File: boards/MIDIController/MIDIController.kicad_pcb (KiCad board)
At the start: 2 copper layers, 29 parts, among them J4 KeyboardCtrl, J5 TechnicsCtrl, J6 StopLeftCtrl, J7 StopRightCtrl, J9 PanelCtrl

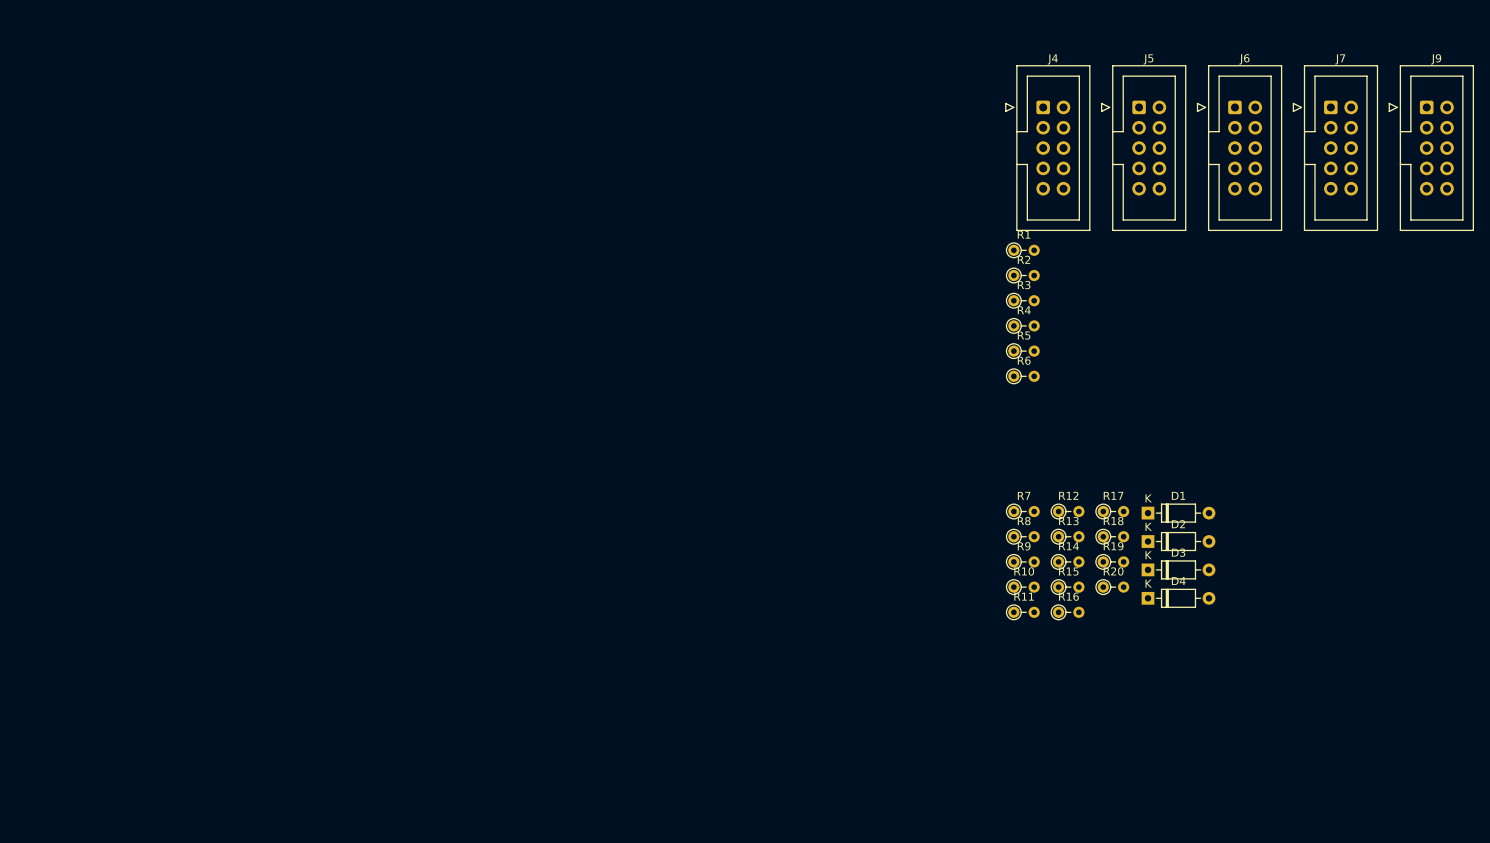
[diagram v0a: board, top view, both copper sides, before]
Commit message: Added Optocoupler and RS232 converter to UART board lines.
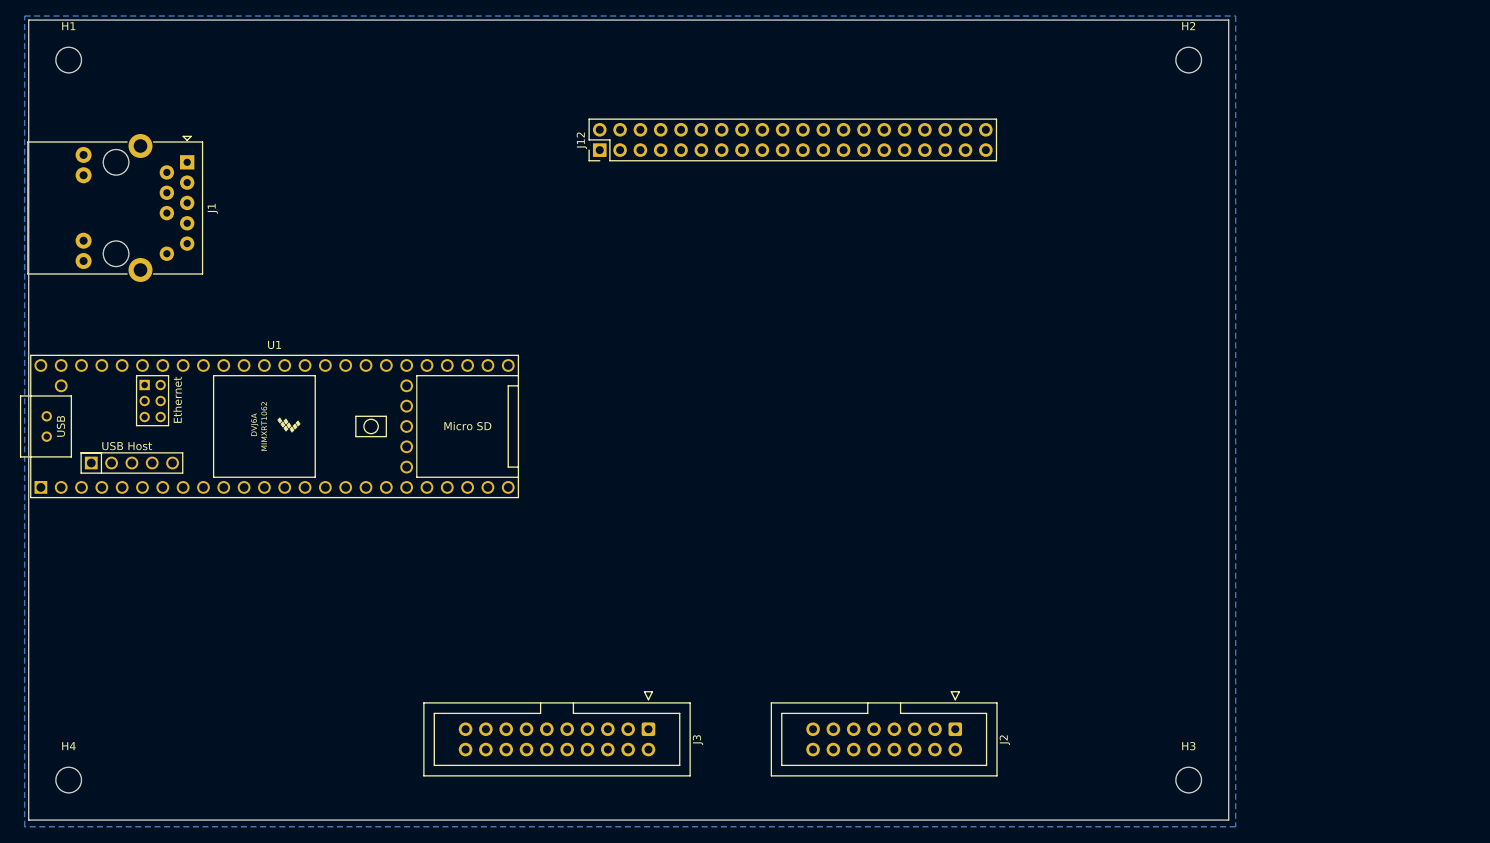
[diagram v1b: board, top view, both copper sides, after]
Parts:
- removed D1, D2, D3, D4: 1N4148, Diode_THT:D_DO-35_SOD27_P7.62mm_Horizontal
- removed J4: KeyboardCtrl, Connector_IDC:IDC-Header_2x05_P2.54mm_Vertical
- removed J5: TechnicsCtrl, Connector_IDC:IDC-Header_2x05_P2.54mm_Vertical
- removed J6: StopLeftCtrl, Connector_IDC:IDC-Header_2x05_P2.54mm_Vertical
- removed J7: StopRightCtrl, Connector_IDC:IDC-Header_2x05_P2.54mm_Vertical
- removed J9: PanelCtrl, Connector_IDC:IDC-Header_2x05_P2.54mm_Vertical
- removed R1, R11, R12, R13, R14, R15, R16, R17, R18, R19, R2, R20, R3, R4, R5, R6: 220, Resistor_THT:R_Axial_DIN0204_L3.6mm_D1.6mm_P2.54mm_Vertical
- removed R10, R7, R8, R9: 10k, Resistor_THT:R_Axial_DIN0204_L3.6mm_D1.6mm_P2.54mm_Vertical
- added H1: MountingHole, MountingHole:MountingHole_3.2mm_M3, F.Cu at (71.5, 50.2)
- added H2: MountingHole, MountingHole:MountingHole_3.2mm_M3, F.Cu at (211.5, 50.2)
- added H3: MountingHole, MountingHole:MountingHole_3.2mm_M3, F.Cu at (211.5, 140.2)
- added H4: MountingHole, MountingHole:MountingHole_3.2mm_M3, F.Cu at (71.5, 140.2)
- added J1: RJ45_Abracon_ARJP11A-MASA-B-A-EMU2, Connector_RJ:RJ45_Abracon_ARJP11A-MA_Horizontal, F.Cu at (86.4, 63.0)
- added J12: Raspberry_Pi_2_3, Connector_PinHeader_2.54mm:PinHeader_2x20_P2.54mm_Vertical, F.Cu at (137.9, 61.5)
- added J2: MIDICon, Connector_IDC:IDC-Header_2x08_P2.54mm_Vertical, F.Cu at (182.4, 133.9)
- added J3: IO_Boards, Connector_IDC:IDC-Header_2x10_P2.54mm_Vertical, F.Cu at (144.0, 133.9)
- added U1: Teensy4.1, Teensy:Teensy41, F.Cu at (97.3, 96.0)
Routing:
- added copper zone on B.Cu, net GND
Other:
- board outline added: 150 x 100 mm

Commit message: Updated MidiController PCB footprints
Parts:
- removed J12: Raspberry_Pi_2_3, Connector_PinHeader_2.54mm:PinHeader_2x20_P2.54mm_Vertical
- added C1: 100nF, Capacitor_THT:C_Disc_D4.3mm_W1.9mm_P5.00mm, F.Cu at (177.1, 92.5)
- added C2: 10uF, Capacitor_THT:CP_Radial_D7.5mm_P2.50mm, F.Cu at (179.0, 86.2)
- added C3: 100nF, Capacitor_THT:C_Disc_D4.3mm_W1.9mm_P5.00mm, F.Cu at (167.0, 93.1)
- added J4: USB_A, Connector_USB:USB_A_Molex_67643_Horizontal, F.Cu at (79.5, 119.4)
- added J5: I2S_Data, Connector_PinHeader_2.54mm:PinHeader_1x08_P2.54mm_Vertical, F.Cu at (163.1, 84.0)
- added J6: I2C_Pwr, Connector_PinHeader_2.54mm:PinHeader_1x08_P2.54mm_Vertical, F.Cu at (153.9, 84.3)
- added J7: Raspberry_Pi_2_3, Connector_PinHeader_2.54mm:PinHeader_2x20_P2.54mm_Vertical, F.Cu at (137.4, 61.5)
- added J8: RJ45_Amphenol_RJMG1BD3B8K1ANR, Connector_RJ:RJ45_Amphenol_RJMG1BD3B8K1ANR, F.Cu at (84.1, 64.8)
- added RN1: 1k, Resistor_THT:R_Array_SIP9, F.Cu at (151.7, 126.0)
- J1: value RJ45_Abracon_ARJP11A-MASA-B-A-EMU2 -> Ctrl; footprint Connector_RJ:RJ45_Abracon_ARJP11A-MA_Horizontal -> Connector_PinHeader_2.54mm:PinHeader_1x03_P2.54mm_Vertical
- moved J1 84.0 mm to (167.7, 84.0), turned to 0 degrees
- moved U1 1.80 mm to (97.0, 94.2)
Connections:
- J1 pad 1: unconnected-(J1-TD+-Pad1) -> Net-(J1-Pin_1)
- J1 pad 2: unconnected-(J1-TD--Pad2) -> Net-(J1-Pin_2)
- J1 pad 3: unconnected-(J1-RD+-Pad3) -> Net-(J1-Pin_3)
- J3 pad 1: /INT1 -> /Int_Panel
- J3 pad 10: /SDA -> +12V
- J3 pad 11: /INT5 -> /Int_Kbd
- J3 pad 12: /SCL -> GND
- J3 pad 14: +3.3V -> GND
- J3 pad 17: /RXD3 -> /RXD4
- J3 pad 18: GND -> +5V
- J3 pad 19: /RXD4 -> /RXD3
- J3 pad 2: +12V -> +3.3V
- J3 pad 20: GND -> +5V
- J3 pad 3: /INT2 -> /Int_StopLeft
- J3 pad 4: +12V -> /SDA
- J3 pad 5: /INT4 -> /Int_StopRight
- J3 pad 6: +5V -> /SCL
- J3 pad 7: /INT3 -> /Int_ToeStud
- J3 pad 8: +5V -> +12V
- J3 pad 9: /INT6 -> /Int_Technics
- U1 pad 12: unconnected-(U1-10_CS_MQSR-Pad12) -> /RPI_CS
- U1 pad 13: unconnected-(U1-11_MOSI_CTX1-Pad13) -> /RPI_MOSI
- U1 pad 14: unconnected-(U1-12_MISO_MQSL-Pad14) -> /RPI_MISO
- U1 pad 25: unconnected-(U1-33_MCLK2-Pad25) -> /I2S_MCLK2
- U1 pad 28: /INT6 -> /Int_Panel
- U1 pad 29: /INT5 -> /Int_ToeStud
- U1 pad 30: /INT4 -> /Int_StopLeft
- U1 pad 31: /INT3 -> /Int_StopRight
- U1 pad 32: /INT2 -> /Int_Technics
- U1 pad 33: /INT1 -> /Int_Kbd
- U1 pad 35: unconnected-(U1-13_SCK_LED-Pad35) -> /RPI_SCLK
- U1 pad 4: unconnected-(U1-2_OUT2-Pad4) -> /I2S_OUT2
- U1 pad 5: unconnected-(U1-3_LRCLK2-Pad5) -> /I2S_LRCLK2
- U1 pad 50: unconnected-(U1-VBAT-Pad50) -> Net-(BT1-+)
- U1 pad 52: GND -> Net-(J1-Pin_3)
- U1 pad 53: unconnected-(U1-PROGRAM-Pad53) -> Net-(J1-Pin_2)
- U1 pad 54: unconnected-(U1-ON_OFF-Pad54) -> Net-(J1-Pin_1)
- U1 pad 55: unconnected-(U1-5V-Pad55) -> Net-(J4-VBUS)
- U1 pad 56: unconnected-(U1-D--Pad56) -> Net-(J4-D-)
- U1 pad 57: unconnected-(U1-D+-Pad57) -> Net-(J4-D+)
- U1 pad 58: unconnected-(U1-GND-Pad58) -> Net-(J4-GND)
- U1 pad 59: unconnected-(U1-GND-Pad59) -> Net-(J4-GND)
- U1 pad 6: unconnected-(U1-4_BCLK2-Pad6) -> /I2S_BCLK2
- U1 pad 60: unconnected-(U1-R+-Pad60) -> /Eth_R+
- U1 pad 61: unconnected-(U1-LED-Pad61) -> /Eth_LED
- U1 pad 62: unconnected-(U1-T--Pad62) -> /Eth_T-
- U1 pad 63: unconnected-(U1-T+-Pad63) -> /Eth_T+
- U1 pad 64: unconnected-(U1-GND-Pad64) -> /Eth_Gnd
- U1 pad 65: unconnected-(U1-R--Pad65) -> /Eth_R-
- U1 pad 7: unconnected-(U1-5_IN2-Pad7) -> /I2S_IN2

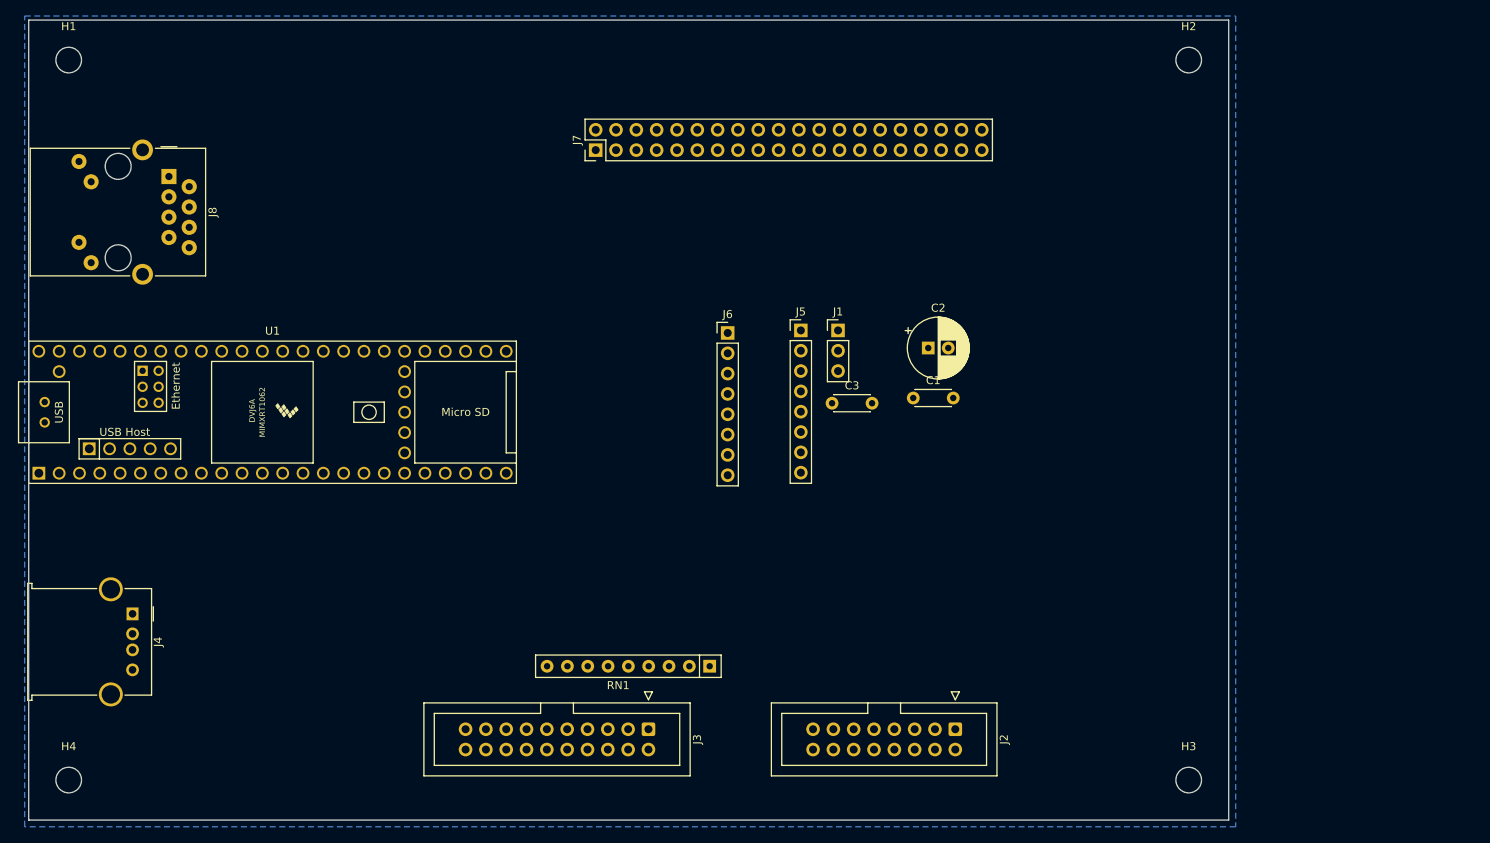
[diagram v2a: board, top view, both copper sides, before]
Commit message: Added CR2032 holder footprint, allow routing between pins
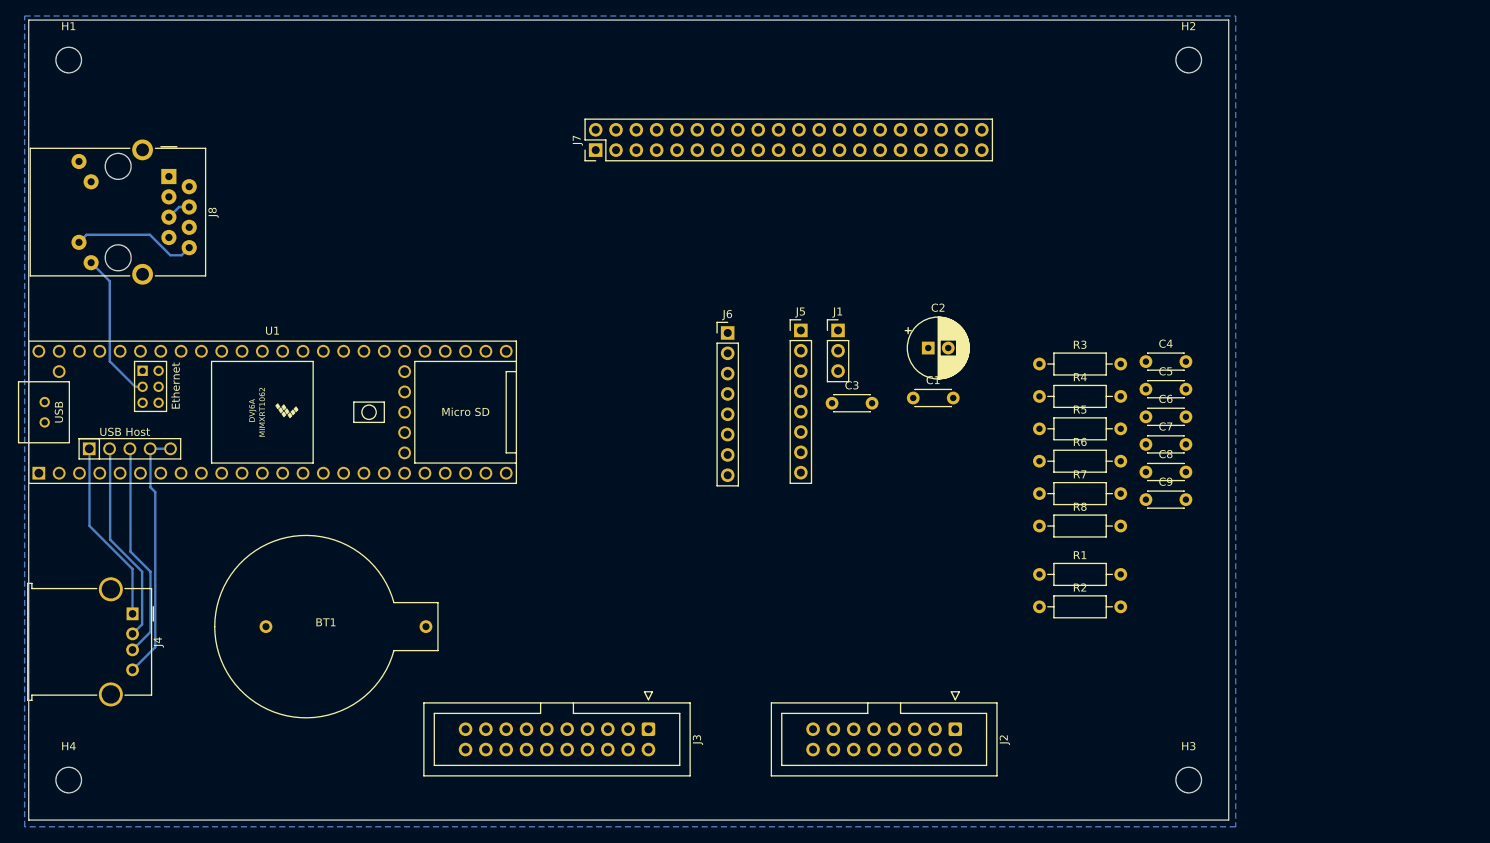
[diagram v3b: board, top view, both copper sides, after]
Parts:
- removed RN1: 1k, Resistor_THT:R_Array_SIP9
- added BT1: Battery_Cell, Custom_Footprints:BatteryHolder_Holder_CR2032, F.Cu at (103.7, 121.0)
- added C4: 10nF, Capacitor_THT:C_Disc_D4.3mm_W1.9mm_P5.00mm, F.Cu at (206.2, 87.9)
- added C5: 10nF, Capacitor_THT:C_Disc_D4.3mm_W1.9mm_P5.00mm, F.Cu at (206.2, 91.4)
- added C6: 10nF, Capacitor_THT:C_Disc_D4.3mm_W1.9mm_P5.00mm, F.Cu at (206.2, 94.8)
- added C7: 10nF, Capacitor_THT:C_Disc_D4.3mm_W1.9mm_P5.00mm, F.Cu at (206.2, 98.3)
- added C8: 10nF, Capacitor_THT:C_Disc_D4.3mm_W1.9mm_P5.00mm, F.Cu at (206.2, 101.7)
- added C9: 10nF, Capacitor_THT:C_Disc_D4.3mm_W1.9mm_P5.00mm, F.Cu at (206.2, 105.2)
- added R1: 4k7, Resistor_THT:R_Axial_DIN0207_L6.3mm_D2.5mm_P10.16mm_Horizontal, F.Cu at (192.9, 114.5)
- added R2: 4k7, Resistor_THT:R_Axial_DIN0207_L6.3mm_D2.5mm_P10.16mm_Horizontal, F.Cu at (192.9, 118.6)
- added R3: 100, Resistor_THT:R_Axial_DIN0207_L6.3mm_D2.5mm_P10.16mm_Horizontal, F.Cu at (192.9, 88.2)
- added R4: 100, Resistor_THT:R_Axial_DIN0207_L6.3mm_D2.5mm_P10.16mm_Horizontal, F.Cu at (192.9, 92.3)
- added R5: 100, Resistor_THT:R_Axial_DIN0207_L6.3mm_D2.5mm_P10.16mm_Horizontal, F.Cu at (192.9, 96.3)
- added R6: 100, Resistor_THT:R_Axial_DIN0207_L6.3mm_D2.5mm_P10.16mm_Horizontal, F.Cu at (192.9, 100.4)
- added R7: 100, Resistor_THT:R_Axial_DIN0207_L6.3mm_D2.5mm_P10.16mm_Horizontal, F.Cu at (192.9, 104.4)
- added R8: 100, Resistor_THT:R_Axial_DIN0207_L6.3mm_D2.5mm_P10.16mm_Horizontal, F.Cu at (192.9, 108.5)
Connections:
- J3 pad 1: /Int_Panel -> Net-(J3-Pin_1)
- J3 pad 11: /Int_Kbd -> Net-(J3-Pin_11)
- J3 pad 3: /Int_StopLeft -> Net-(J3-Pin_3)
- J3 pad 5: /Int_StopRight -> Net-(J3-Pin_5)
- J3 pad 7: /Int_ToeStud -> Net-(J3-Pin_7)
- J3 pad 9: /Int_Technics -> Net-(J3-Pin_9)
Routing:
- net Net-(J4-GND): track 0.00 -> 31.6 mm
- net Net-(J4-D+): track 0.00 -> 27.1 mm
- net Net-(J4-D-): track 0.00 -> 25.3 mm
- net Net-(J4-VBUS): track 0.00 -> 22.9 mm
- net /Eth_LED: track 0.00 -> 18.7 mm
- net /Eth_Gnd: track 0.00 -> 15.6 mm
- net Net-(J8-RCT): track 0.00 -> 3.07 mm
